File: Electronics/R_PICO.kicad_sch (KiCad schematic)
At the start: 14 parts, among them U1 R-785.0-0.5, U2 VL53L0CXV0DH1, U3 VL53L0CXV0DH1, U4 VL53L0CXV0DH1, U5 VL53L0CXV0DH1, U6 TB6612FNG

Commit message: corrected electronic schema, added adc support
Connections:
- net scl1: now also A1.10 (GPIO7); no longer A1.14 (GPIO10)
- net sda1: now also A1.9 (GPIO6); no longer A1.12 (GPIO9)
- net at U4.5 (XSHUT): now also A1.6 (GPIO4)
- net at U2.5 (XSHUT): now also A1.7 (GPIO5)
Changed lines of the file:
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@@
+	)
+	(junction
+		(at 77.47 80.01)
+		(diameter 0)
+		(color 0 0 0 0)
 	)
 	(junction
@@
 	)
 	(junction
-		(at 74.93 77.47)
-		(diameter 0)
-		(color 0 0 0 0)
-	)
-	(junction
 		(at 194.31 67.31)
 		(diameter 0)
@@
 	)
 	(junction
-		(at 77.47 80.01)
+		(at 74.93 77.47)
 		(diameter 0)
 		(color 0 0 0 0)
@@
 	(wire
 		(pts
+			(xy 191.77 114.3) (xy 119.38 114.3)
+		)
+		(stroke
+			(width 0)
+			(type default)
+		)
+	)
+	(wire
+		(pts
 			(xy 52.07 26.67) (xy 52.07 53.34)
 		)
@@
 	(wire
 		(pts
+			(xy 119.38 67.31) (xy 129.54 67.31)
+		)
+		(stroke
+			(width 0)
+			(type default)
+		)
+	)
+	(wire
+		(pts
 			(xy 93.98 158.75) (xy 93.98 157.48)
 		)
@@
 	(wire
 		(pts
-			(xy 77.47 80.01) (xy 129.54 80.01)
-		)
-		(stroke
-			(width 0)
-			(type default)
-		)
-	)
-	(wire
-		(pts
-			(xy 74.93 77.47) (xy 129.54 77.47)
+			(xy 83.82 77.47) (xy 74.93 77.47)
+		)
+		(stroke
+			(width 0)
+			(type default)
+		)
+	)
+	(wire
+		(pts
+			(xy 119.38 64.77) (xy 129.54 64.77)
 		)
 		(stroke
@@
 	(wire
 		(pts
+			(xy 119.38 66.04) (xy 119.38 64.77)
+		)
+		(stroke
+			(width 0)
+			(type default)
+		)
+	)
+	(wire
+		(pts
 			(xy 36.83 77.47) (xy 74.93 77.47)
 		)
@@
 	(wire
 		(pts
+			(xy 201.93 72.39) (xy 201.93 62.23)
+		)
+		(stroke
+			(width 0)
+			(type default)
+		)
+	)
+	(wire
+		(pts
 			(xy 99.06 97.79) (xy 99.06 101.6)
 		)
@@
 	(wire
 		(pts
+			(xy 119.38 67.31) (xy 119.38 114.3)
+		)
+		(stroke
+			(width 0)
+			(type default)
+		)
+	)
+	(wire
+		(pts
 			(xy 199.39 148.59) (xy 191.77 148.59)
 		)
@@
 	(wire
 		(pts
+			(xy 129.54 72.39) (xy 86.36 72.39)
+		)
+		(stroke
+			(width 0)
+			(type default)
+		)
+	)
+	(wire
+		(pts
+			(xy 129.54 69.85) (xy 83.82 69.85)
+		)
+		(stroke
+			(width 0)
+			(type default)
+		)
+	)
+	(wire
+		(pts
 			(xy 194.31 62.23) (xy 194.31 67.31)
 		)
@@
 	(wire
 		(pts
+			(xy 86.36 72.39) (xy 86.36 80.01)
+		)
+		(stroke
+			(width 0)
+			(type default)
+		)
+	)
+	(wire
+		(pts
 			(xy 106.68 121.92) (xy 110.49 121.92)
 		)
@@
 	(wire
 		(pts
+			(xy 191.77 72.39) (xy 201.93 72.39)
+		)
+		(stroke
+			(width 0)
+			(type default)
+		)
+	)
+	(wire
+		(pts
 			(xy 72.39 132.08) (xy 76.2 132.08)
 		)
@@
 	(wire
 		(pts
+			(xy 83.82 69.85) (xy 83.82 77.47)
+		)
+		(stroke
+			(width 0)
+			(type default)
+		)
+	)
+	(wire
+		(pts
 			(xy 256.54 139.7) (xy 256.54 148.59)
 		)
@@
 	(wire
 		(pts
+			(xy 86.36 80.01) (xy 77.47 80.01)
+		)
+		(stroke
+			(width 0)
+			(type default)
+		)
+	)
+	(wire
+		(pts
 			(xy 39.37 66.04) (xy 39.37 80.01)
 		)
@@
 	(wire
 		(pts
+			(xy 82.55 66.04) (xy 119.38 66.04)
+		)
+		(stroke
+			(width 0)
+			(type default)
+		)
+	)
+	(wire
+		(pts
 			(xy 72.39 124.46) (xy 76.2 124.46)
+		)
+		(stroke
+			(width 0)
+			(type default)
+		)
+	)
+	(wire
+		(pts
+			(xy 191.77 72.39) (xy 191.77 114.3)
 		)
 		(stroke
@@
 	)
 	(label "scl1"
-		(at 121.92 80.01 0)
+		(at 111.76 72.39 0)
 		(effects
 			(font
@@
 	)
 	(label "sda1"
-		(at 124.46 77.47 0)
+		(at 111.76 69.85 0)
 		(effects
 			(font

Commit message: added starter scheme
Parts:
- added Starter1: ~, symbol Own:Starter
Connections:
- net 3V3: now also U6.19 (STBY), Starter1. (START)
- net GND: now also Starter1. (START)
- net KILL: now reaches A1.11 (GPIO8)
- net KILL: now also Starter1. (START)
- net START: now reaches A1.12 (GPIO9)
- net START: now also Starter1. (START)
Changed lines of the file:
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@@
+		)
+	)
+	(global_label "KILL"
+		(shape input)
+		(at 146.05 130.81 90)
+		(fields_autoplaced yes)
+		(effects
+			(font
+				(size 1.27 1.27)
+			)
+			(justify left)
+		)
+		(property "Intersheetrefs" "${INTERSHEET_REFS}"
+			(at 146.05 123.8938 90)
+			(effects
+				(font
+					(size 1.27 1.27)
+				)
+				(justify left)
+				(hide yes)
+			)
+		)
+	)
+	(global_label "START"
+		(shape input)
+		(at 129.54 77.47 180)
+		(fields_autoplaced yes)
+		(effects
+			(font
+				(size 1.27 1.27)
+			)
+			(justify right)
+		)
+		(property "Intersheetrefs" "${INTERSHEET_REFS}"
+			(at 121.0515 77.47 0)
+			(effects
+				(font
+					(size 1.27 1.27)
+				)
+				(justify right)
+				(hide yes)
+			)
+		)
+	)
+	(global_label "KILL"
+		(shape input)
+		(at 129.54 74.93 180)
+		(fields_autoplaced yes)
+		(effects
+			(font
+				(size 1.27 1.27)
+			)
+			(justify right)
+		)
+		(property "Intersheetrefs" "${INTERSHEET_REFS}"
+			(at 122.6238 74.93 0)
+			(effects
+				(font
+					(size 1.27 1.27)
+				)
+				(justify right)
+				(hide yes)
+			)
+		)
+	)
+	(global_label "START"
+		(shape input)
+		(at 148.59 130.81 90)
+		(fields_autoplaced yes)
+		(effects
+			(font
+				(size 1.27 1.27)
+			)
+			(justify left)
+		)
+		(property "Intersheetrefs" "${INTERSHEET_REFS}"
+			(at 148.59 122.3215 90)
+			(effects
+				(font
+					(size 1.27 1.27)
+				)
+				(justify left)
+				(hide yes)
+			)
 		)
 	)
@@
 		)
 	)
+	(hierarchical_label "3V3"
+		(shape bidirectional)
+		(at 76.2 116.84 180)
+		(effects
+			(font
+				(size 1.27 1.27)
+			)
+			(justify right)
+		)
+	)
 	(hierarchical_label "5V"
 		(shape bidirectional)
@@
 			)
 			(justify right)
+		)
+	)
+	(hierarchical_label "3V3"
+		(shape bidirectional)
+		(at 140.97 130.81 90)
+		(effects
+			(font
+				(size 1.27 1.27)
+			)
+			(justify left)
 		)
 	)
@@
 	)
 	(symbol
+		(lib_id "Own:Starter")
+		(at 143.51 128.27 0)
+		(unit 1)
+		(exclude_from_sim no)
+		(in_bom yes)
+		(on_board yes)
+		(dnp no)
+		(fields_autoplaced yes)
+		(property "Reference" "Starter1"
+			(at 151.13 137.1599 0)
+			(effects
+				(font
+					(size 1.27 1.27)
+				)
+				(justify left)
+			)
+		)
+		(property "Value" "~"
+			(at 151.13 139.6999 0)
+			(effects
+				(font
+					(size 1.27 1.27)
+				)
+				(justify left)
+			)
+		)
+		(property "Footprint" ""
+			(at 143.51 128.27 0)
+			(effects
+				(font
+					(size 1.27 1.27)
+				)
+				(hide yes)
+			)
+		)
+		(property "Datasheet" ""
+			(at 143.51 128.27 0)
+			(effects
+				(font
+					(size 1.27 1.27)
+				)
+				(hide yes)
+			)
+		)
+		(property "Description" ""
+			(at 143.51 128.27 0)
+			(effects
+				(font
+					(size 1.27 1.27)
+				)
+				(hide yes)
+			)
+		)
+		(pin ""
+		)
+		(pin ""
+		)
+		(pin ""
+		)
+		(pin ""
+		)
+		(instances
+			(project ""
+				(path "/8d834d26-b607-404e-affc-aead426ecb0a"
+					(reference "Starter1")
+					(unit 1)
+				)
+			)
+		)
+	)
+	(symbol
 		(lib_id "power:GND")
 		(at 240.03 142.24 0)
@@
 					(unit 1)
 				)
+			)
+		)
+	)
+	(symbol
+		(lib_id "power:GND")
+		(at 143.51 130.81 180)
+		(unit 1)
+		(exclude_from_sim no)
+		(in_bom yes)
+		(on_board yes)
+		(dnp no)
+		(fields_autoplaced yes)
+		(property "Reference" "#PWR012"
+			(at 143.51 124.46 0)
+			(effects
+				(font
+					(size 1.27 1.27)
+				)
+				(hide yes)
+			)
+		)
+		(property "Value" "GND"
+			(at 143.51 125.73 0)
+			(effects
+				(font
+					(size 1.27 1.27)
+				)
+			)
+		)
+		(property "Footprint" ""
+			(at 143.51 130.81 0)
+			(effects
+				(font
+					(size 1.27 1.27)
+				)
+				(hide yes)
+			)
+		)
+		(property "Datasheet" ""
+			(at 143.51 130.81 0)
+			(effects
+				(font
+					(size 1.27 1.27)
+				)
+				(hide yes)
+			)
+		)
+		(property "Description" "Power symbol creates a global label with name \"GND\" , ground"
+			(at 143.51 130.81 0)
+			(effects
+				(font
+					(size 1.27 1.27)
+				)
+				(hide yes)
+			)
+		)
+		(pin "1"
+		)
+		(instances
+			(project "R_PICO"
+				(path "/8d834d26-b607-404e-affc-aead426ecb0a"
+					(reference "#PWR012")
+					(unit 1)
+				)

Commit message: updated electronics
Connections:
- net 3V3: no longer A1.35 (ADC_VREF)
- net GND: now also U4.12 (GND), U4.3 (GND), U4.4 (GND), U4.6 (GND), U5.12 (GND), U5.3 (GND), U5.4 (GND), U5.6 (GND)
- net at U5.5 (XSHUT): now also A1.5 (GPIO3)
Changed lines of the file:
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@@
+	(wire
+		(pts
+			(xy 100.33 62.23) (xy 100.33 38.1)
+		)
+		(stroke
+			(width 0)
+			(type default)
+		)
+	)
 	(wire
 		(pts
@@
 	(wire
 		(pts
+			(xy 55.88 38.1) (xy 55.88 66.04)
+		)
+		(stroke
+			(width 0)
+			(type default)
+		)
+	)
+	(wire
+		(pts
 			(xy 187.96 27.94) (xy 190.5 27.94)
 		)
@@
 	(wire
 		(pts
+			(xy 129.54 62.23) (xy 100.33 62.23)
+		)
+		(stroke
+			(width 0)
+			(type default)
+		)
+	)
+	(wire
+		(pts
 			(xy 191.77 72.39) (xy 191.77 114.3)
 		)
@@
 	(wire
 		(pts
+			(xy 100.33 38.1) (xy 55.88 38.1)
+		)
+		(stroke
+			(width 0)
+			(type default)
+		)
+	)
+	(wire
+		(pts
 			(xy 166.37 27.94) (xy 172.72 27.94)
 		)
@@
 		(pts
 			(xy 125.73 87.63) (xy 129.54 87.63)
+		)
+		(stroke
+			(width 0)
+			(type default)
+		)
+	)
+	(wire
+		(pts
+			(xy 55.88 66.04) (xy 44.45 66.04)
 		)
 		(stroke
@@
 		(shape bidirectional)
 		(at 226.06 31.75 90)
-		(effects
-			(font
-				(size 1.27 1.27)
-			)
-			(justify left)
-		)
-	)
-	(hierarchical_label "3V3"
-		(shape bidirectional)
-		(at 176.53 77.47 0)
 		(effects
 			(font
@@
 	(symbol
 		(lib_id "power:GND")
+		(at 52.07 55.88 0)
+		(unit 1)
+		(exclude_from_sim no)
+		(in_bom yes)
+		(on_board yes)
+		(dnp no)
+		(fields_autoplaced yes)
+		(property "Reference" "#PWR014"
+			(at 52.07 62.23 0)
+			(effects
+				(font
+					(size 1.27 1.27)
+				)
+				(hide yes)
+			)
+		)
+		(property "Value" "GND"
+			(at 52.07 60.96 0)
+			(effects
+				(font
+					(size 1.27 1.27)
+				)
+			)
+		)
+		(property "Footprint" ""
+			(at 52.07 55.88 0)
+			(effects
+				(font
+					(size 1.27 1.27)
+				)
+				(hide yes)
+			)
+		)
+		(property "Datasheet" ""
+			(at 52.07 55.88 0)
+			(effects
+				(font
+					(size 1.27 1.27)
+				)
+				(hide yes)
+			)
+		)
+		(property "Description" "Power symbol creates a global label with name \"GND\" , ground"
+			(at 52.07 55.88 0)
+			(effects
+				(font
+					(size 1.27 1.27)
+				)
+				(hide yes)
+			)
+		)
+		(pin "1"
+		)
+		(instances
+			(project "R_PICO"
+				(path "/8d834d26-b607-404e-affc-aead426ecb0a"
+					(reference "#PWR014")
+					(unit 1)
+				)
+			)
+		)
+	)
+	(symbol
+		(lib_id "power:GND")
 		(at 266.7 134.62 0)
 		(unit 1)
@@
 					(unit 1)
 				)
+			)
+		)
+	)
+	(symbol
+		(lib_id "power:GND")
+		(at 90.17 55.88 0)
+		(unit 1)
+		(exclude_from_sim no)
+		(in_bom yes)
+		(on_board yes)
+		(dnp no)
+		(fields_autoplaced yes)
+		(property "Reference" "#PWR013"
+			(at 90.17 62.23 0)
+			(effects
+				(font
+					(size 1.27 1.27)
+				)
+				(hide yes)
+			)
+		)
+		(property "Value" "GND"
+			(at 90.17 60.96 0)
+			(effects
+				(font
+					(size 1.27 1.27)
+				)
+			)
+		)
+		(property "Footprint" ""
+			(at 90.17 55.88 0)
+			(effects
+				(font
+					(size 1.27 1.27)
+				)
+				(hide yes)
+			)
+		)
+		(property "Datasheet" ""
+			(at 90.17 55.88 0)
+			(effects
+				(font
+					(size 1.27 1.27)
+				)
+				(hide yes)
+			)
+		)
+		(property "Description" "Power symbol creates a global label with name \"GND\" , ground"
+			(at 90.17 55.88 0)
+			(effects
+				(font
+					(size 1.27 1.27)
+				)
+				(hide yes)
+			)
+		)
+		(pin "1"
+		)
+		(instances
+			(project "R_PICO"
+				(path "/8d834d26-b607-404e-affc-aead426ecb0a"
+					(reference "#PWR013")
+					(unit 1)
+				)

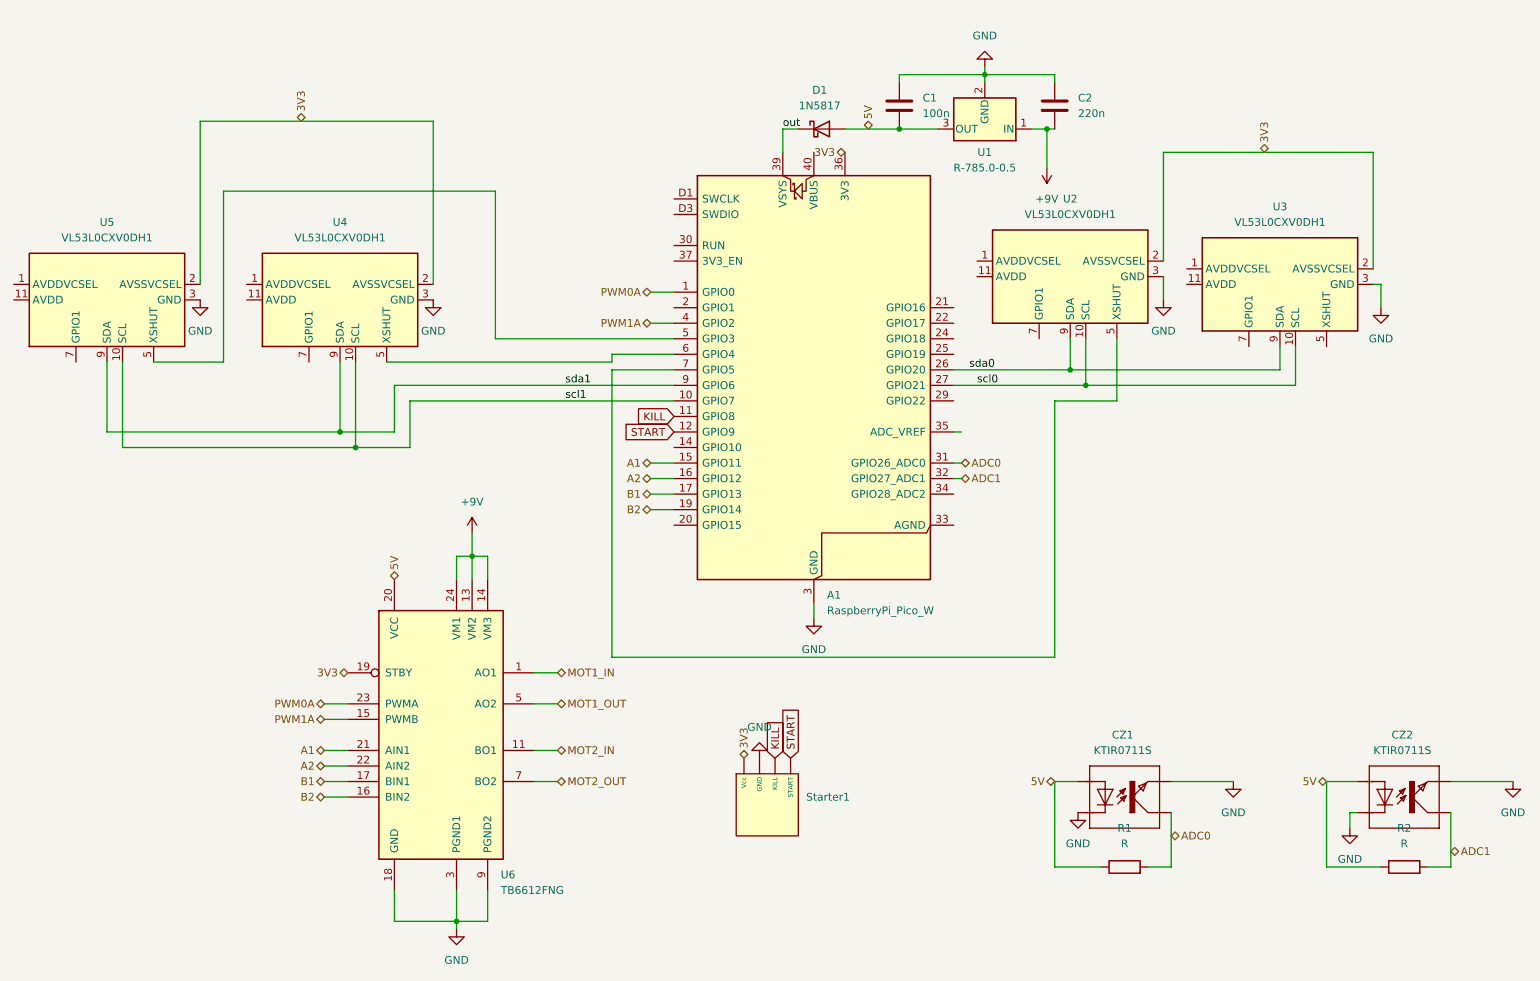
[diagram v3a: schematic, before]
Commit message: FIX: Changed Electronics schema
Changed footprints of VL53L0X, KTIRs, and TB6612FNG. Amended electronics
schema to match breakout boards.
TODO: PCB schematic
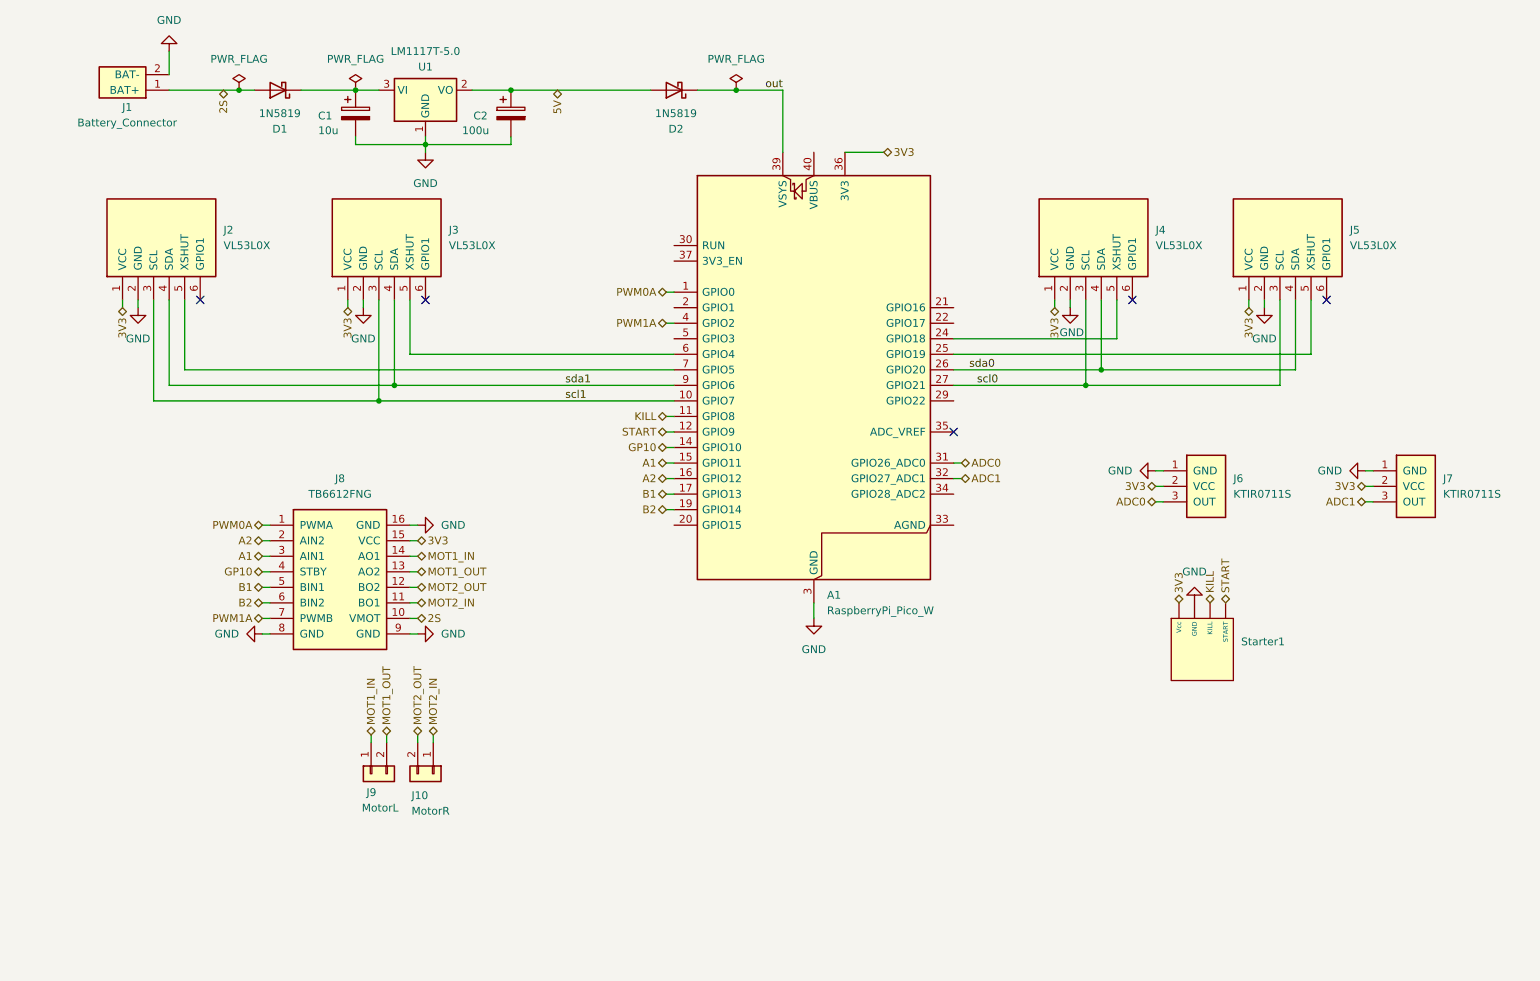
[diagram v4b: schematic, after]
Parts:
- removed C1: 100n, symbol Device:C
- removed C2: 220n, symbol Device:C
- removed CZ1, CZ2: KTIR0711S, KTIR0711S-TOP, symbol KTIR0711S:KTIR0711S
- removed R1, R2: R, symbol Device:R
- removed U1: R-785.0-0.5, Converter_DCDC:Converter_DCDC_RECOM_R-78E-0.5_THT, symbol Regulator_Switching:R-781.5-0.5
- removed U2, U3, U4, U5: VL53L0CXV0DH1, Sensor_Distance:ST_VL53L1x, symbol Sensor_Distance:VL53L0CXV0DH1
- removed U6: TB6612FNG, Package_SO:SSOP-24_5.3x8.2mm_P0.65mm, symbol Driver_Motor:TB6612FNG
- added C1: 10u, Capacitor_THT:CP_Radial_D5.0mm_P2.00mm, symbol Device:C_Polarized
- added C2: 100u, Capacitor_THT:CP_Radial_D6.3mm_P2.50mm, symbol Device:C_Polarized
- added D1: 1N5819, Diode_THT:D_DO-41_SOD81_P10.16mm_Horizontal, symbol Diode:1N5817
- added J1: Battery_Connector, Connector_PinHeader_2.54mm:PinHeader_1x02_P2.54mm_Vertical, symbol ARENT_SYMBOLS_LIB:Battery_Connector
- added J10: MotorR, TerminalBlock_Phoenix:TerminalBlock_Phoenix_MKDS-1,5-2_1x02_P5.00mm_Horizontal, symbol Connector_Generic:Conn_01x02
- added J2, J3, J4, J5: VL53L0X, Connector_PinHeader_2.54mm:PinHeader_1x06_P2.54mm_Vertical, symbol ARENT_SYMBOLS_LIB:VL53L0X
- added J6, J7: KTIR0711S, Connector_PinHeader_2.54mm:PinHeader_1x03_P2.54mm_Vertical, symbol ARENT_SYMBOLS_LIB:KTIR0711S
- added J8: TB6612FNG, ARENT_FOOTPRINT_LIB:TB6612FNG_Polulu_Breakout, symbol ARENT_SYMBOLS_LIB:TB6612FNG
- added J9: MotorL, TerminalBlock_Phoenix:TerminalBlock_Phoenix_MKDS-1,5-2_1x02_P5.00mm_Horizontal, symbol Connector_Generic:Conn_01x02
- added U1: LM1117T-5.0, Package_TO_SOT_THT:TO-220-3_Vertical, symbol Regulator_Linear:LM1117T-5.0
- A1: footprint Module:RaspberryPi_Pico_W_SMD_HandSolder -> Module:RaspberryPi_Pico_Common_THT; symbol MCU_Module:RaspberryPi_Pico_W_Debug -> MCU_Module:RaspberryPi_Pico_W
- D2: renamed from D1; value 1N5817 -> 1N5819
- Starter1: footprint (none) -> Connector_PinHeader_2.54mm:PinHeader_1x04_P2.54mm_Vertical
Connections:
- net 3V3: now also J2.1 (VCC), J3.1 (VCC), J4.1 (VCC), J5.1 (VCC), J6.2 (VCC), J7.2 (VCC), J8.15 (VCC)
- net 5V: now also C2.1, U1.2 (VO)
- net A1: now also J8.3 (AIN1)
- net A2: now also J8.2 (AIN2)
- net ADC0: now also J6.3 (OUT)
- net ADC1: now also J7.3 (OUT)
- net B1: now also J8.5 (BIN1)
- net B2: now also J8.6 (BIN2)
- net GND: now also C1.2, C2.2, J1.2 (BAT-), J2.2 (GND), J3.2 (GND), J4.2 (GND), J5.2 (GND), J6.1 (GND), J7.1 (GND), J8.16 (GND), J8.8 (GND), J8.9 (GND), U1.1 (GND); no longer A1.D2 (GND)
- net MOT1_IN: now also J8.14 (AO1), J9.1 (Pin_1)
- net MOT1_OUT: now also J8.13 (AO2), J9.2 (Pin_2)
- net MOT2_IN: now also J10.1 (Pin_1), J8.11 (BO1)
- net MOT2_OUT: now also J10.2 (Pin_2), J8.12 (BO2)
- net PWM0A: now also J8.1 (PWMA)
- net PWM1A: now also J8.7 (PWMB)
- net scl0: now also J4.3 (SCL), J5.3 (SCL)
- net scl1: now also J2.3 (SCL), J3.3 (SCL)
- net sda0: now also J4.4 (SDA), J5.4 (SDA)
- net sda1: now also J2.4 (SDA), J3.4 (SDA)
- net at A1.6 (GPIO4): now also J3.5 (XSHUT)
- net at A1.7 (GPIO5): now also J2.5 (XSHUT)
- net GP10: now reaches A1.14 (GPIO10)
- net GP10: now also J8.4 (STBY)
- net at A1.24 (GPIO18): now also J4.5 (XSHUT)
- net at A1.25 (GPIO19): now also J5.5 (XSHUT)
- new net: C1.1, D1.1 (K), U1.3 (VI)
- new net 2S: D1.2 (A), J1.1 (BAT+), J8.10 (VMOT)
- no-connect marks 0 -> 5
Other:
- moved on the sheet: D2, Starter1
